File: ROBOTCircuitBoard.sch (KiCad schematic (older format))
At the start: 16 parts, among them J1 DB15_HighDensity_MountingHoles, J2 DB15_HighDensity_MountingHoles, P1 CONN_01X03, P2 CONN_01X04, P5 CONN_01X05, U1 MCP2551-I/P

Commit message: fixing things more
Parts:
- added Y?: Crystal 32.768kHz, symbol Crystal
- added Y?: Crystal 16MHz, symbol Crystal
- P?: value CONN_01X02 -> Pushbutton NO
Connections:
- net labels added: Prog
- wire segments 27 -> 41
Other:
- note added: "Why is this greyed out on the diagram?\n"
- note removed: "Pushbutton NO\n"
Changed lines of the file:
@@
 P 4950 6900
 F 0 "P?" H 4950 7050 50  0000 C CNN
-F 1 "CONN_01X02" V 5050 6900 50  0000 C CNN
+F 1 "Pushbutton NO" V 5050 6900 50  0000 C CNN
 F 2 "" H 4950 6900 50  0000 C CNN
 F 3 "" H 4950 6900 50  0000 C CNN
@@
 $EndComp
 Wire Wire Line
-	4750 6850 4450 6850
+	4400 6850 4750 6850
 Wire Wire Line
 	4450 6850 4450 6050
@@
 L +3.3V #PWR?
 U 1 1 58D8302A
-P 4700 5650
-F 0 "#PWR?" H 4700 5500 50  0001 C CNN
-F 1 "+3.3V" H 4700 5790 50  0000 C CNN
-F 2 "" H 4700 5650 50  0000 C CNN
-F 3 "" H 4700 5650 50  0000 C CNN
-	1    4700 5650
-	0    -1   -1   0
+P 3800 3550
+F 0 "#PWR?" H 3800 3400 50  0001 C CNN
+F 1 "+3.3V" H 3800 3690 50  0000 C CNN
+F 2 "" H 3800 3550 50  0000 C CNN
+F 3 "" H 3800 3550 50  0000 C CNN
+	1    3800 3550
+	0    1    1    0
 $EndComp
 Text Label 3650 6650 0    60   ~ 0
@@
 L GND #PWR?
 U 1 1 59320A11
-P 4350 4650
-F 0 "#PWR?" H 4350 4400 50  0001 C CNN
-F 1 "GND" H 4350 4500 50  0000 C CNN
-F 2 "" H 4350 4650 50  0000 C CNN
-F 3 "" H 4350 4650 50  0000 C CNN
-	1    4350 4650
+P 4900 7150
+F 0 "#PWR?" H 4900 6900 50  0001 C CNN
+F 1 "GND" H 4900 7000 50  0000 C CNN
+F 2 "" H 4900 7150 50  0000 C CNN
+F 3 "" H 4900 7150 50  0000 C CNN
+	1    4900 7150
 	0    -1   -1   0
 $EndComp
@@
 Text Label 4250 7350 0    60   ~ 0
 P
-Text Notes 5000 7300 1    60   ~ 0
-Pushbutton NO\n
+$Comp
+L Crystal Y?
+U 1 1 596D6B80
+P 3650 5900
+F 0 "Y?" H 3650 6050 50  0000 C CNN
+F 1 "Crystal 32.768kHz" H 3650 5750 50  0000 C CNN
+F 2 "" H 3650 5900 50  0000 C CNN
+F 3 "" H 3650 5900 50  0000 C CNN
+	1    3650 5900
+	0    -1   -1   0
+$EndComp
+Wire Wire Line
+	1350 6450 1250 6450
+Wire Wire Line
+	1250 6450 1250 6350
+Wire Wire Line
+	1250 6350 1100 6350
+Wire Wire Line
+	1350 6550 1250 6550
+Wire Wire Line
+	1250 6550 1250 6650
+Wire Wire Line
+	1250 6650 1100 6650
+Connection ~ 4450 6850
+Text Label 4400 6850 2    60   ~ 0
+Prog
+Wire Wire Line
+	4900 7150 4400 7150
+Wire Wire Line
+	4400 7150 4400 6700
+Text Label 4400 6700 2    60   ~ 0
+GND
+Text Notes 2650 5850 0    60   ~ 0
+Why is this greyed out on the diagram?\n
+$Comp
+L Crystal Y?
+U 1 1 596D7C7C
+P 1100 6500
+F 0 "Y?" H 1100 6650 50  0000 C CNN
+F 1 "Crystal 16MHz" H 1100 6350 50  0000 C CNN
+F 2 "" H 1100 6500 50  0000 C CNN
+F 3 "" H 1100 6500 50  0000 C CNN
+	1    1100 6500
+	0    1    1    0
+$EndComp
+Wire Wire Line
+	3650 3550 3650 3750
+Wire Wire Line
+	3650 3550 3800 3550
+Wire Wire Line
+	3650 3750 4350 3750
+Wire Wire Line
+	4350 3750 4350 4500
+Wire Wire Line
+	4350 4500 4700 4500
+Wire Wire Line
+	4700 4500 4700 5650
 $EndSCHEMATC

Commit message: Added more components
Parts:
- removed C?: CP1, symbol CP1
- removed Y?: Crystal 32.768kHz, symbol Crystal
- added C? (x3): CP 0.1uF, symbol CP
- added C?: CP 2.2uF, symbol CP
- added C? (x3): 0.1uF, symbol CP
- added C?: 2.2uF, symbol CP
- added D? (x2): D, symbol D
- added L?: L Ferrite, symbol L
- added R?: R_Small 470, symbol R_Small
- L?: value L -> L Ferrite
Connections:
- net labels added: 3.3v, AREF, VBAT
- net labels removed: +3.3V, Prog
- wire segments 41 -> 57
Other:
- note added: "3.3V"
- note added: "AGND"
- note added: "AREF"
- note added: "GND\n"
- note added: "Prog\n"
- note added: "VBAT"
- note removed: "Find Inductor\n"
- note removed: "Why is this greyed out on the diagram?\n"
- moved on the sheet: L?

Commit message: Fixed standardization and other issues
Made grounds point downwards for standardization
Fixed an issue with AREF and AGND not being on either side of a capacitor
Fixed some incorrectly placed traces and labels
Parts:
- P?: symbol USB_OTG -> USB_OTG-RESCUE-ROBOTCircuitBoard
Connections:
- net labels added: +3.3V, AGND
- net labels removed: 3.3v
- wire segments 57 -> 82
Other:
- note removed: "AGND"
- note removed: "AREF"
- note removed: "D0 – D33 are the Digital Ports\n"
- moved on the sheet: P?

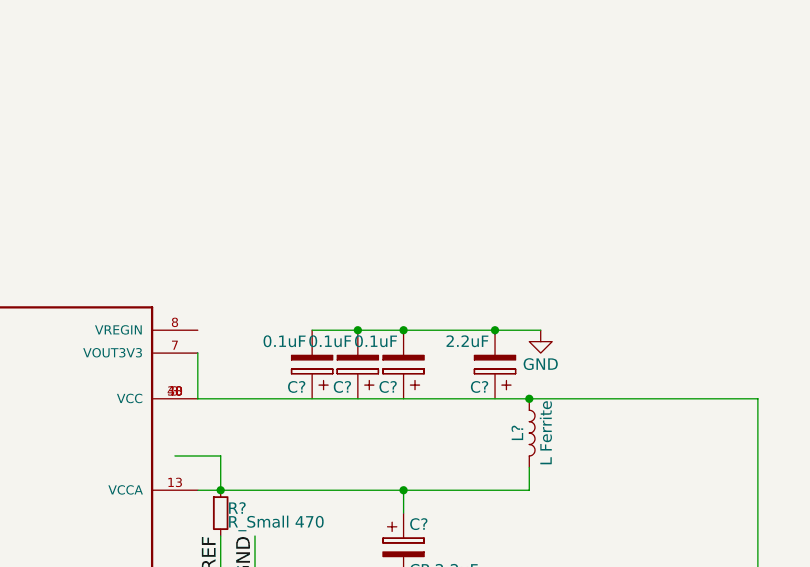
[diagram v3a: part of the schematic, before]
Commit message: added the lp38691
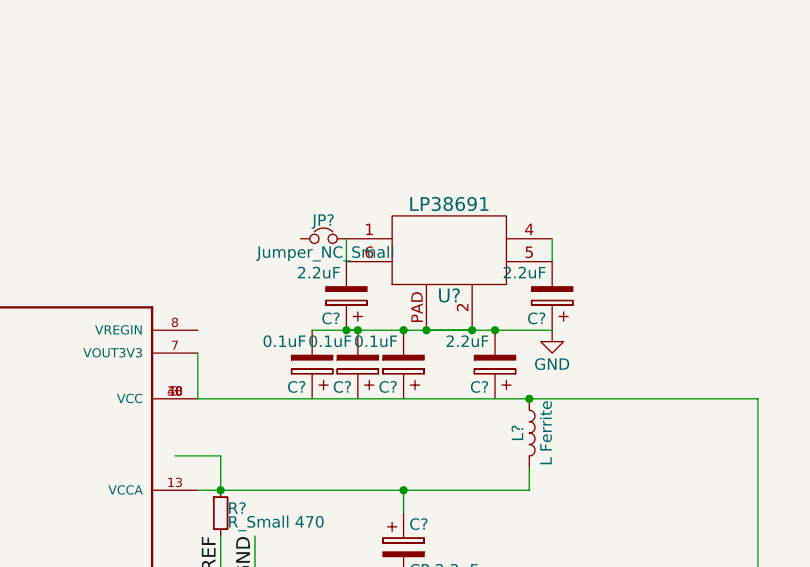
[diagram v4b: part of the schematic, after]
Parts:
- added C? (x2): 2.2uF, symbol CP
- added JP?: Jumper_NC_Small, symbol Jumper_NC_Small
- added U?: LP38691, symbol LP38691
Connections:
- wire segments 82 -> 86
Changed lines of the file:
@@
 LIBS:contrib
 LIBS:valves
+LIBS:lp38691
 LIBS:ROBOTCircuitBoard-cache
 EELAYER 25 0
@@
 L GND #PWR?
 U 1 1 597D909A
-P 5150 3450
-F 0 "#PWR?" H 5150 3200 50  0001 C CNN
-F 1 "GND" H 5150 3300 50  0000 C CNN
-F 2 "" H 5150 3450 50  0000 C CNN
-F 3 "" H 5150 3450 50  0000 C CNN
-	1    5150 3450
+P 5200 3450
+F 0 "#PWR?" H 5200 3200 50  0001 C CNN
+F 1 "GND" H 5200 3300 50  0000 C CNN
+F 2 "" H 5200 3450 50  0000 C CNN
+F 3 "" H 5200 3450 50  0000 C CNN
+	1    5200 3450
 	1    0    0    -1
 $EndComp
@@
 	4700 6350 4700 6450
 Wire Wire Line
-	4150 3450 5150 3450
+	4150 3450 5200 3450
 Connection ~ 4950 3450
 Connection ~ 4550 3450
@@
 	5450 7000 5450 6800
 Connection ~ 5950 6900
+$Comp
+L LP38691 U?
+U 1 1 5980B365
+P 4750 3100
+F 0 "U?" H 4750 2900 60  0000 C CNN
+F 1 "LP38691" H 4750 3300 60  0000 C CNN
+F 2 "" H 4750 3100 60  0001 C CNN
+F 3 "" H 4750 3100 60  0001 C CNN
+	1    4750 3100
+	1    0    0    -1
+$EndComp
+Wire Wire Line
+	4650 3450 4850 3450
+Connection ~ 4850 3450
+Connection ~ 4650 3450
+Wire Wire Line
+	5200 3050 5200 3150
+$Comp
+L CP C?
+U 1 1 5980B97B
+P 5200 3300
+F 0 "C?" H 5225 3400 50  0000 L CNN
+F 1 "2.2uF" H 5225 3200 50  0000 L CNN
+F 2 "" H 5238 3150 50  0000 C CNN
+F 3 "" H 5200 3300 50  0000 C CNN
+	1    5200 3300
+	-1   0    0    1
+$EndComp
+$Comp
+L CP C?
+U 1 1 5980C1A0
+P 4300 3300
+F 0 "C?" H 4325 3400 50  0000 L CNN
+F 1 "2.2uF" H 4325 3200 50  0000 L CNN
+F 2 "" H 4338 3150 50  0000 C CNN
+F 3 "" H 4300 3300 50  0000 C CNN
+	1    4300 3300
+	-1   0    0    1
+$EndComp
+Wire Wire Line
+	4300 3450 4350 3450
+Connection ~ 4300 3450
+Wire Wire Line
+	4300 3050 4300 3150
+$Comp
+L Jumper_NC_Small JP?
+U 1 1 5980C3AE
+P 4200 3050
+F 0 "JP?" H 4200 3130 50  0000 C CNN
+F 1 "Jumper_NC_Small" H 4210 2990 50  0000 C CNN
+F 2 "" H 4200 3050 50  0000 C CNN
+F 3 "" H 4200 3050 50  0000 C CNN
+	1    4200 3050
+	1    0    0    -1
+$EndComp
 $EndSCHEMATC

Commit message: finished schematic draft 1
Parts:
- added C?: 2.2uF, symbol CP
- added F?: Fuse, symbol Fuse
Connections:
- wire segments 86 -> 90
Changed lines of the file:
@@
 	4700 6350 4700 6450
 Wire Wire Line
-	4150 3450 5200 3450
+	3800 3450 5200 3450
 Connection ~ 4950 3450
 Connection ~ 4550 3450
@@
 	1    0    0    -1
 $EndComp
+$Comp
+L Fuse F?
+U 1 1 5980A7D8
+P 3950 3050
+F 0 "F?" V 4030 3050 50  0000 C CNN
+F 1 "Fuse" V 3875 3050 50  0000 C CNN
+F 2 "" V 3880 3050 50  0000 C CNN
+F 3 "" H 3950 3050 50  0000 C CNN
+	1    3950 3050
+	0    1    1    0
+$EndComp
+Connection ~ 4150 3450
+$Comp
+L CP C?
+U 1 1 5980AC81
+P 3800 3300
+F 0 "C?" H 3825 3400 50  0000 L CNN
+F 1 "2.2uF" H 3825 3200 50  0000 L CNN
+F 2 "" H 3838 3150 50  0000 C CNN
+F 3 "" H 3800 3300 50  0000 C CNN
+	1    3800 3300
+	-1   0    0    1
+$EndComp
+Wire Wire Line
+	3800 2850 3800 3150
+Wire Wire Line
+	3800 2850 6250 2850
+Wire Wire Line
+	6250 2850 6250 5200
+Wire Wire Line
+	6250 5200 5900 5200
+Connection ~ 3800 3050
 $EndSCHEMATC

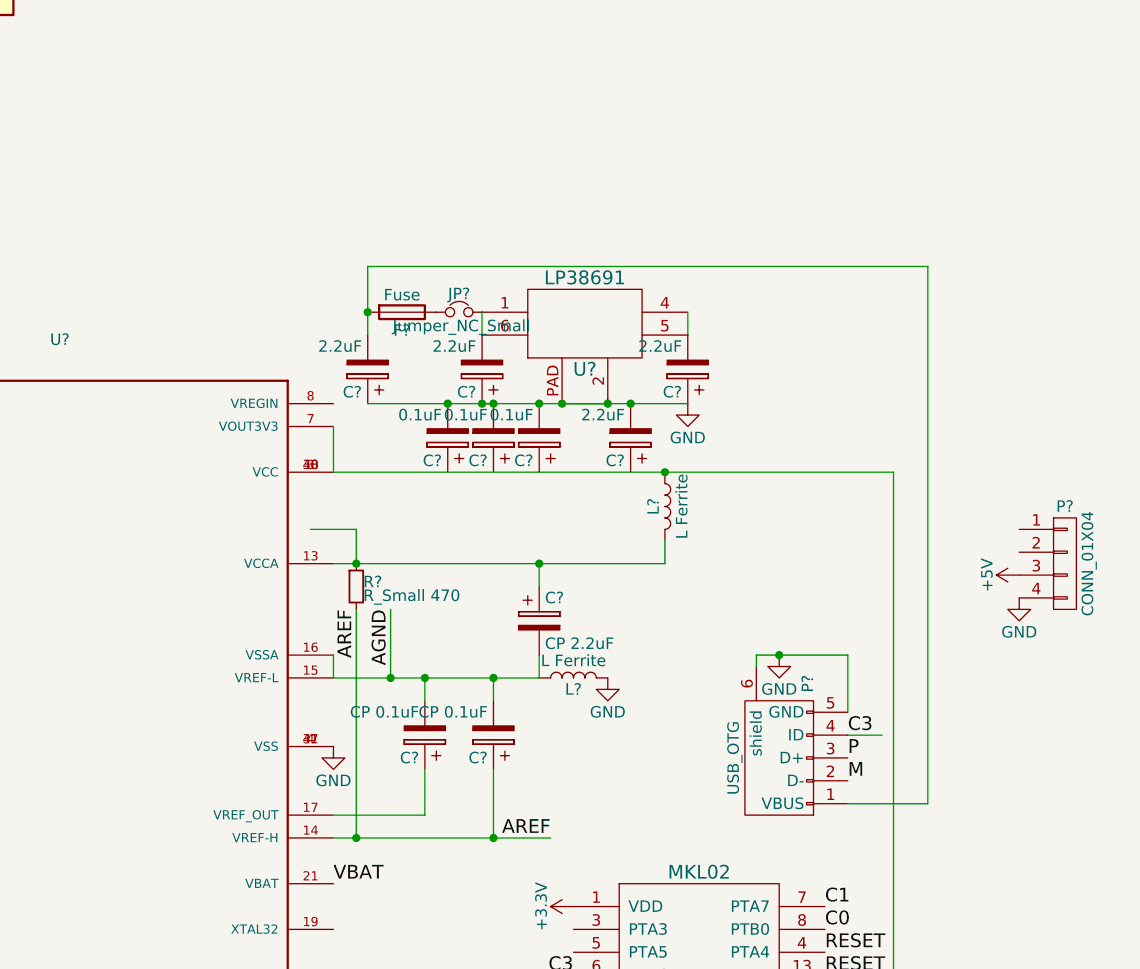
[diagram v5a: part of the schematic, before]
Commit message: Fixed capacitor, organization, and VIN issues Fixed issues with pins 4 and 5 on the LP38691 not being connected to 3.3VDC becuase of capacitor Took out long traces and reorganized Made a VIN trace for power without USB connection
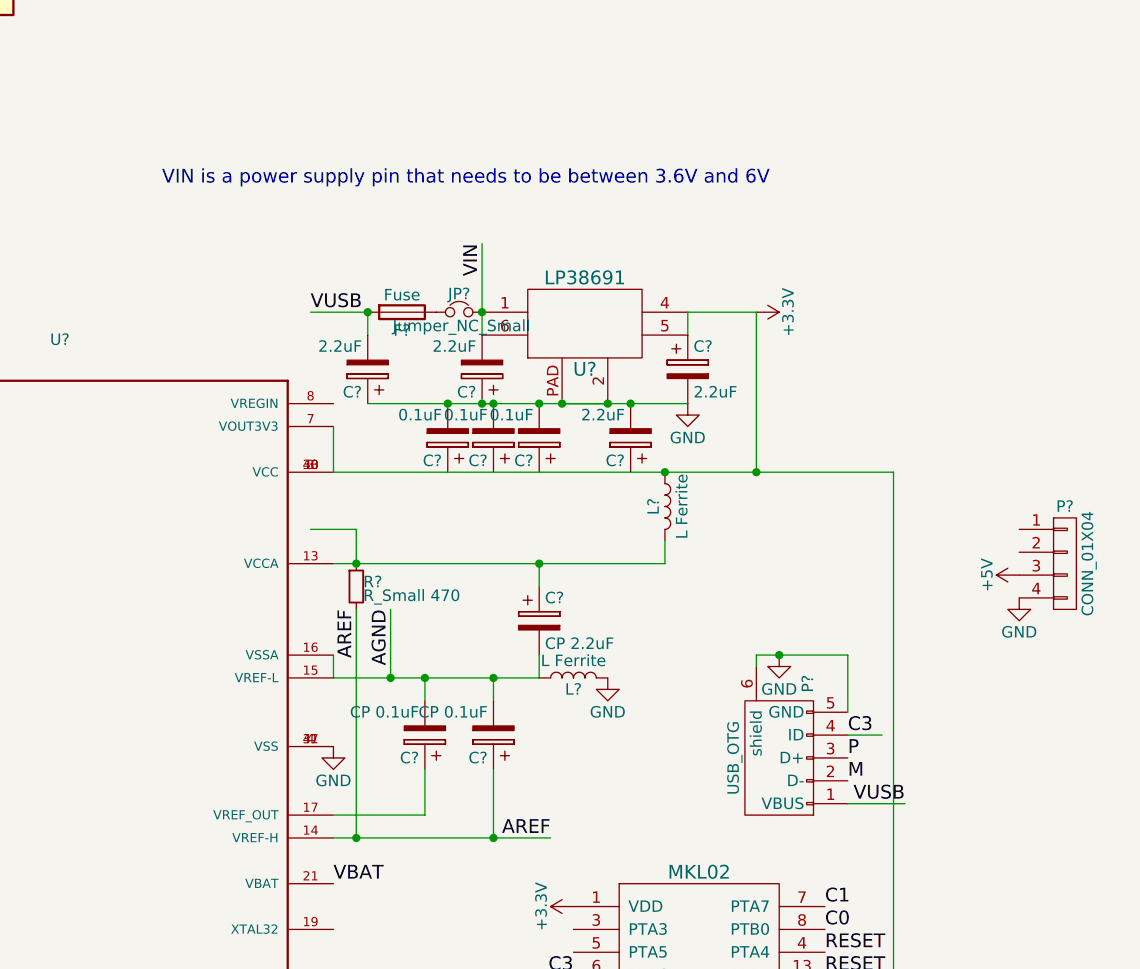
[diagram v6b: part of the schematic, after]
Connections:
- net labels added: VIN, VUSB
- wire segments 90 -> 91
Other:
- note added: "VIN is a power supply pin that needs to be between 3.6V and 6V"
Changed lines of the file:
@@
 F 3 "" H 5200 3300 50  0000 C CNN
 	1    5200 3300
-	-1   0    0    1
+	1    0    0    -1
 $EndComp
 $Comp
@@
 Connection ~ 4300 3450
 Wire Wire Line
-	4300 3050 4300 3150
+	4300 2750 4300 3150
 $Comp
 L Jumper_NC_Small JP?
@@
 $EndComp
 Wire Wire Line
-	3800 2850 3800 3150
+	3800 3050 3800 3150
+Connection ~ 3800 3050
 Wire Wire Line
-	3800 2850 6250 2850
+	5200 3050 5500 3050
+$Comp
+L +3.3V #PWR?
+U 1 1 59814146
+P 5500 3050
+F 0 "#PWR?" H 5500 2900 50  0001 C CNN
+F 1 "+3.3V" H 5500 3190 50  0000 C CNN
+F 2 "" H 5500 3050 50  0001 C CNN
+F 3 "" H 5500 3050 50  0001 C CNN
+	1    5500 3050
+	0    1    1    0
+$EndComp
 Wire Wire Line
-	6250 2850 6250 5200
+	5500 3050 5500 3750
+Connection ~ 5500 3750
 Wire Wire Line
-	6250 5200 5900 5200
-Connection ~ 3800 3050
+	5900 5200 6150 5200
+Text Label 6150 5200 2    60   ~ 0
+VUSB
+Wire Wire Line
+	3550 3050 3800 3050
+Text Label 3550 3050 0    60   ~ 0
+VUSB
+Connection ~ 4300 3050
+Text Label 4300 2750 3    60   ~ 0
+VIN
+Text Notes 2900 2500 0    60   ~ 0
+VIN is a power supply pin that needs to be between 3.6V and 6V
 $EndSCHEMATC

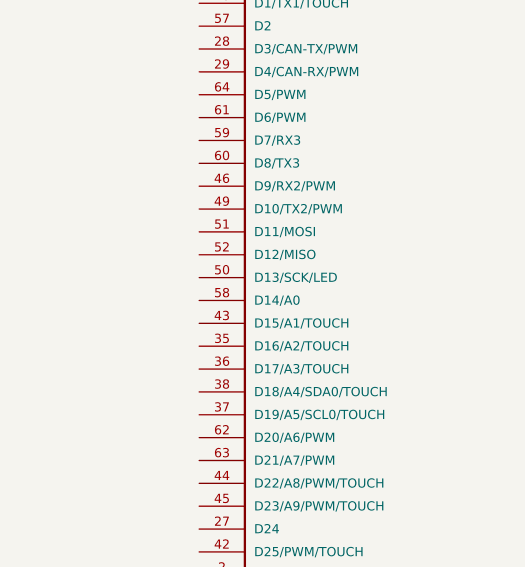
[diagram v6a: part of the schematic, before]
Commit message: Added LED and renamed incorrectly named files Added an LED for debugging purposes Renamed ROBOTCircuitBoard.kicad_pcb to ROBOTCircuitBoard-not_embedded.kicad_pcb because it is the same as a previous board which can be found here: https://github.com/RoboticsTeam4904/2017-Teensy3.6-Board KiCAD qutomatically created ROBOTCircuitBoard.pro which is of no importance and should be ignored
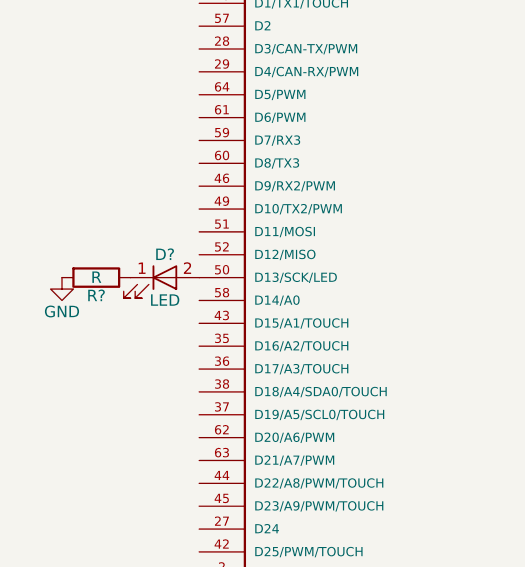
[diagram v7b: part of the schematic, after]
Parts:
- added D?: LED, symbol LED
- added R?: R, symbol R
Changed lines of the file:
@@
 Text Notes 2900 2500 0    60   ~ 0
 VIN is a power supply pin that needs to be between 3.6V and 6V
+$Comp
+L LED D?
+U 1 1 598FA689
+P 1200 4850
+F 0 "D?" H 1200 4950 50  0000 C CNN
+F 1 "LED" H 1200 4750 50  0000 C CNN
+F 2 "" H 1200 4850 50  0001 C CNN
+F 3 "" H 1200 4850 50  0001 C CNN
+	1    1200 4850
+	1    0    0    -1
+$EndComp
+$Comp
+L R R?
+U 1 1 598FA746
+P 900 4850
+F 0 "R?" V 980 4850 50  0000 C CNN
+F 1 "R" V 900 4850 50  0000 C CNN
+F 2 "" V 830 4850 50  0001 C CNN
+F 3 "" H 900 4850 50  0001 C CNN
+	1    900  4850
+	0    1    1    0
+$EndComp
+$Comp
+L GND #PWR?
+U 1 1 598FA803
+P 750 4850
+F 0 "#PWR?" H 750 4600 50  0001 C CNN
+F 1 "GND" H 750 4700 50  0000 C CNN
+F 2 "" H 750 4850 50  0001 C CNN
+F 3 "" H 750 4850 50  0001 C CNN
+	1    750  4850
+	1    0    0    -1
+$EndComp
 $EndSCHEMATC
